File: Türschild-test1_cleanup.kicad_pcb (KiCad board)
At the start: 2 copper layers, 90.2 x 76.2 mm, 97 parts, among them J1 662103130822smt, J3 USB_B_Micro, J4 Conn_01x24_MountingPin, J5 PROG, J6 Conn_01x08_Female, Q1 IRLML2502PbF, U1 BQ25570, U2 BQ27441-G1, U3 ESP32-WROOM-32, U4 CP2102N-A01-GQFN28, U5 LM1117-3.3, U6 WE-TVS-82400102

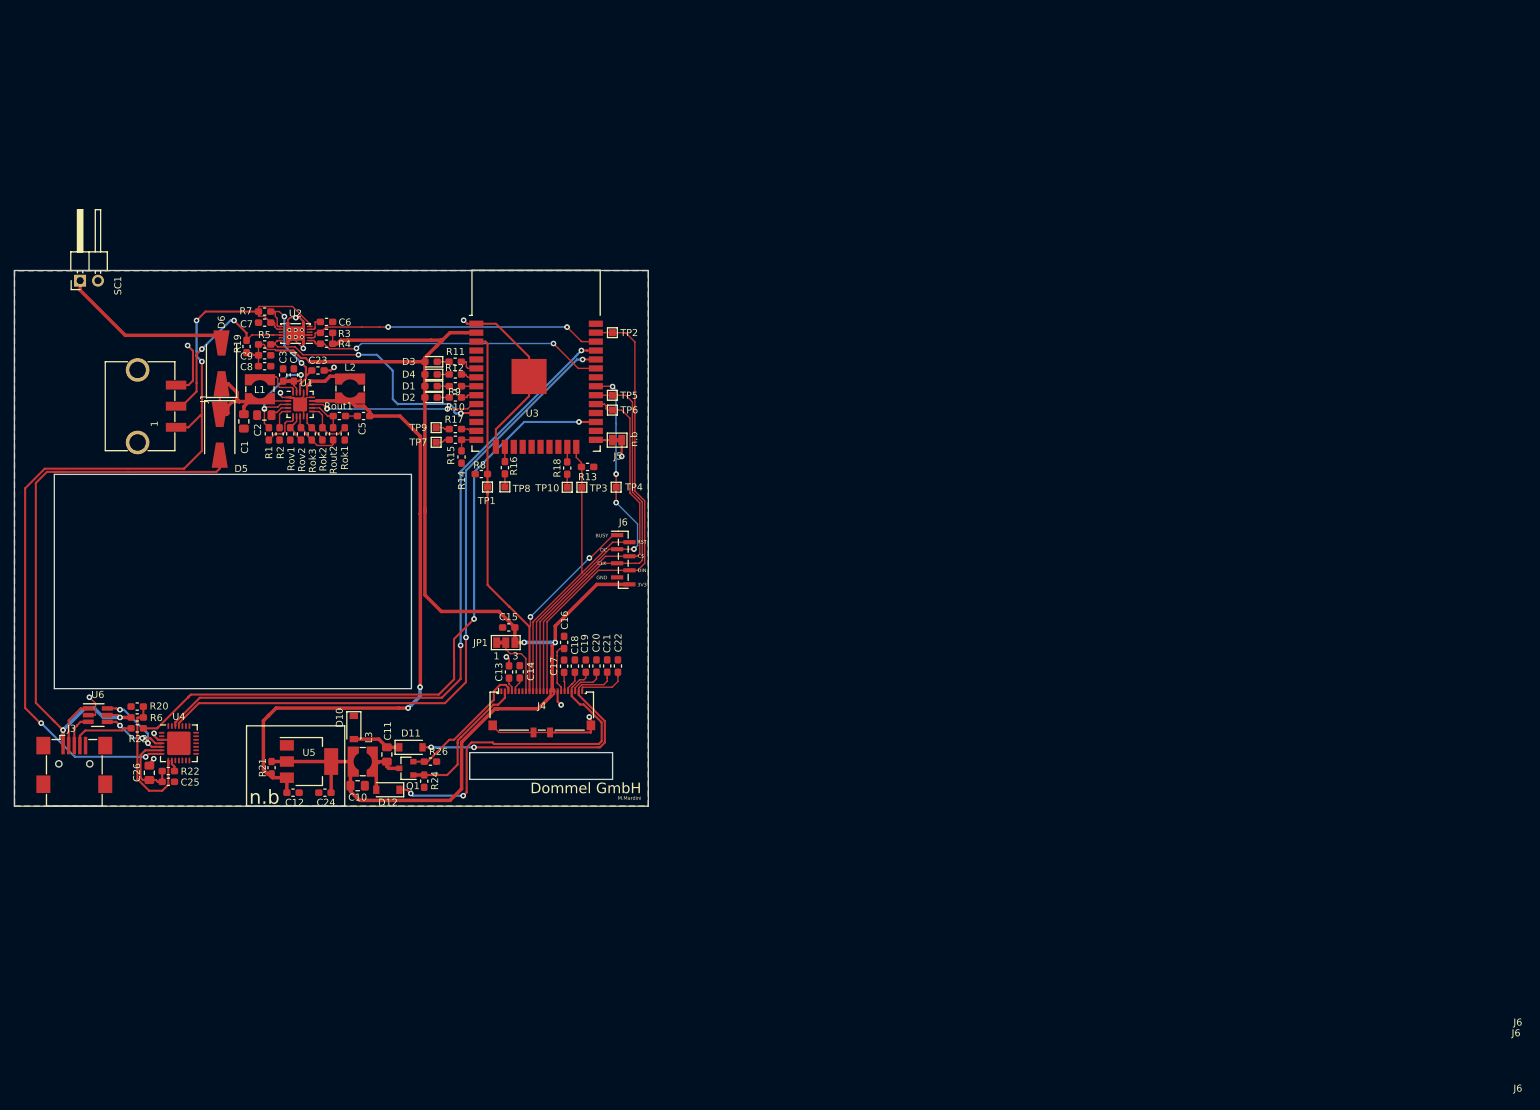
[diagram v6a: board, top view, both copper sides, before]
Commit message: Pull-Ups und Pull-Downs für die beiden USB-Datenleitungen eingebaut. nur 1K5 Wiederstand auf D+ gegen 3V3 wurde bestückt
neue Schaltplan und Layout für korrektour erstellt
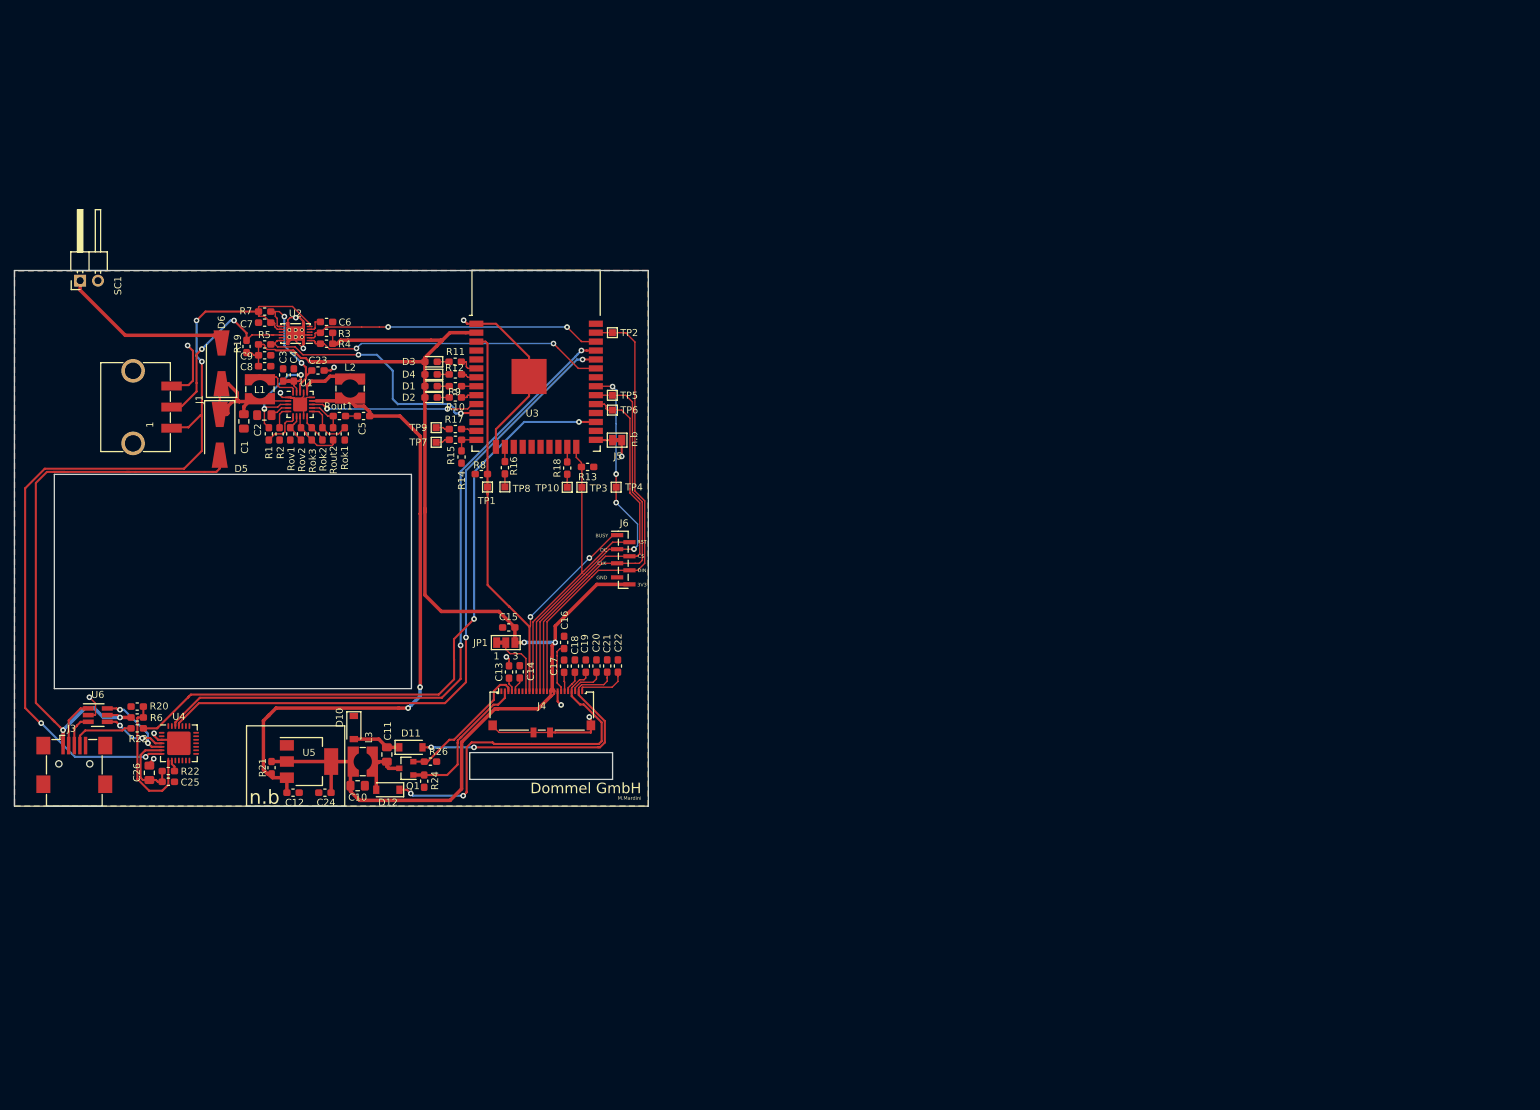
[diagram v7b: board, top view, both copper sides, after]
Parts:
- moved J1 0.66 mm to (123.6, 71.5)
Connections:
- C1 pad 2: GND -> BIN
- C10 pad 1: GND -> BIN
- C12 pad 2: GND -> BIN
- C13 pad 2: GND -> BIN
- C14 pad 2: GND -> BIN
- C15 pad 1: GND -> BIN
- C16 pad 1: GND -> BIN
- C17 pad 1: GND -> BIN
- C18 pad 1: GND -> BIN
- C19 pad 1: GND -> BIN
- C2 pad 2: GND -> BIN
- C20 pad 1: GND -> BIN
- C21 pad 1: GND -> BIN
- C22 pad 1: GND -> BIN
- C23 pad 2: GND -> BIN
- C24 pad 2: GND -> BIN
- C25 pad 2: GND -> BIN
- C26 pad 2: GND -> BIN
- C3 pad 2: GND -> BIN
- C4 pad 2: GND -> BIN
- C5 pad 1: GND -> BIN
- C6 pad 1: GND -> BIN
- C7 pad 2: GND -> BIN
- C8 pad 2: GND -> BIN
- C9 pad 2: GND -> BIN
- D10 pad 1: GND -> BIN
- J1 pad 1: Net-(C7-Pad1) -> Net-(J1-Pad1)
- J1 pad 2: BIN -> Net-(J1-Pad2)
- J1 pad 3: GND -> Net-(J1-Pad3)
- J3 pad 5: GND -> BIN
- J3 pad 6: GND -> BIN
- J4 pad 17: GND -> BIN
- J4 pad MP: GND -> BIN
- J5 pad 2: GND -> BIN
- J6 pad 7: GND -> BIN
- JP1 pad 1: GND -> BIN
- R13 pad 1: GND -> BIN
- R14 pad 2: GND -> BIN
- R2 pad 1: GND -> BIN
- R20 pad 1: GND -> BIN
- R24 pad 1: GND -> BIN
- R26 pad 2: GND -> BIN
- R8 pad 1: GND -> BIN
- Rok1 pad 1: GND -> BIN
- Rout1 pad 1: GND -> BIN
- Rov1 pad 1: GND -> BIN
- SC1 pad 2: GND -> BIN
- U1 pad 1: GND -> BIN
- U1 pad 15: GND -> BIN
- U1 pad 17: GND -> BIN
- U1 pad 21: GND -> BIN
- U1 pad 9: GND -> BIN
- U2 pad 13: GND -> BIN
- U2 pad 3: GND -> BIN
- U3 pad 1: GND -> BIN
- U3 pad 15: GND -> BIN
- U3 pad 38: GND -> BIN
- U3 pad 39: GND -> BIN
- U4 pad 29: GND -> BIN
- U4 pad 3: GND -> BIN
- U5 pad 1: GND -> BIN
- U6 pad 2: GND -> BIN
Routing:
- net GND: track 87.8 -> 0.00 mm, vias 13 -> 0
- net BIN: track 25.5 -> 105.3 mm, vias 2 -> 14
- net Net-(J1-Pad3): track 0.00 -> 7.98 mm, vias 0 -> 1
- added copper zone on B.Cu, net BIN
- added copper zone on F.Cu, net BIN
- removed copper zone on B.Cu, net GND
- removed copper zone on F.Cu, net GND
